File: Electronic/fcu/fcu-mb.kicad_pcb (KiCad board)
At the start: 2 copper layers, 114.3 x 71.1 mm, 48 parts, among them U1 MAX7219, U101 Connector-FPC-50pins, U2 MAX7219, U3 MAX7219

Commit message: Update fcu schemas and libraries
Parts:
- added J1: Conn_Coaxial_Power, Connector_Wire:SolderWirePad_1x02_P3.81mm_Drill1mm, F.Cu at (52.1, 123.8)
- moved R4 21.7 mm to (83.2, 118.7)
- moved R5 21.7 mm to (83.2, 122.6)
- moved R11 3.18 mm to (73.0, 115.6)
- moved R15 3.17 mm to (83.2, 111.8)
- moved U1 1.91 mm to (73.7, 79.4)
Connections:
- A1 pad 27: +5V -> Net-(A1-Pad27)
- A1 pad 30: Net-(A1-Pad30) -> +5V
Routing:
- net Dr3SegA: track 117.9 -> 174.4 mm, vias 2 -> 1
- net Dr3SegE: track 119.4 -> 97.1 mm
- net Dr3SegD: track 138.0 -> 154.5 mm, vias 1 -> 2
- net GND: track 271.1 -> 256.0 mm, vias 1 -> 0
- net Dr3SegB: track 107.4 -> 92.4 mm, vias 1 -> 2
- net Net-(R1-Pad2): track 47.9 -> 61.7 mm, vias 1 -> 0
- net speedAltF: track 36.3 -> 49.9 mm
- net BTN_GRP_2: track 154.8 -> 141.5 mm
- net hdgVsA: track 31.9 -> 44.6 mm
- net Dr3Dig5: track 38.7 -> 50.4 mm, vias 1 -> 2
- net speedAltDig3: track 39.1 -> 50.7 mm, vias 1 -> 0
- net speedAltDig5: track 59.0 -> 70.6 mm
- net Net-(K_AP2-Pad4): track 43.3 -> 54.7 mm
- net Net-(R17-Pad1): track 41.6 -> 52.3 mm, vias 0 -> 1
- net BTN_GRP_1: track 177.3 -> 166.8 mm
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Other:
- board size 114.3 x 71.1 mm -> 114.3 x 67.9 mm

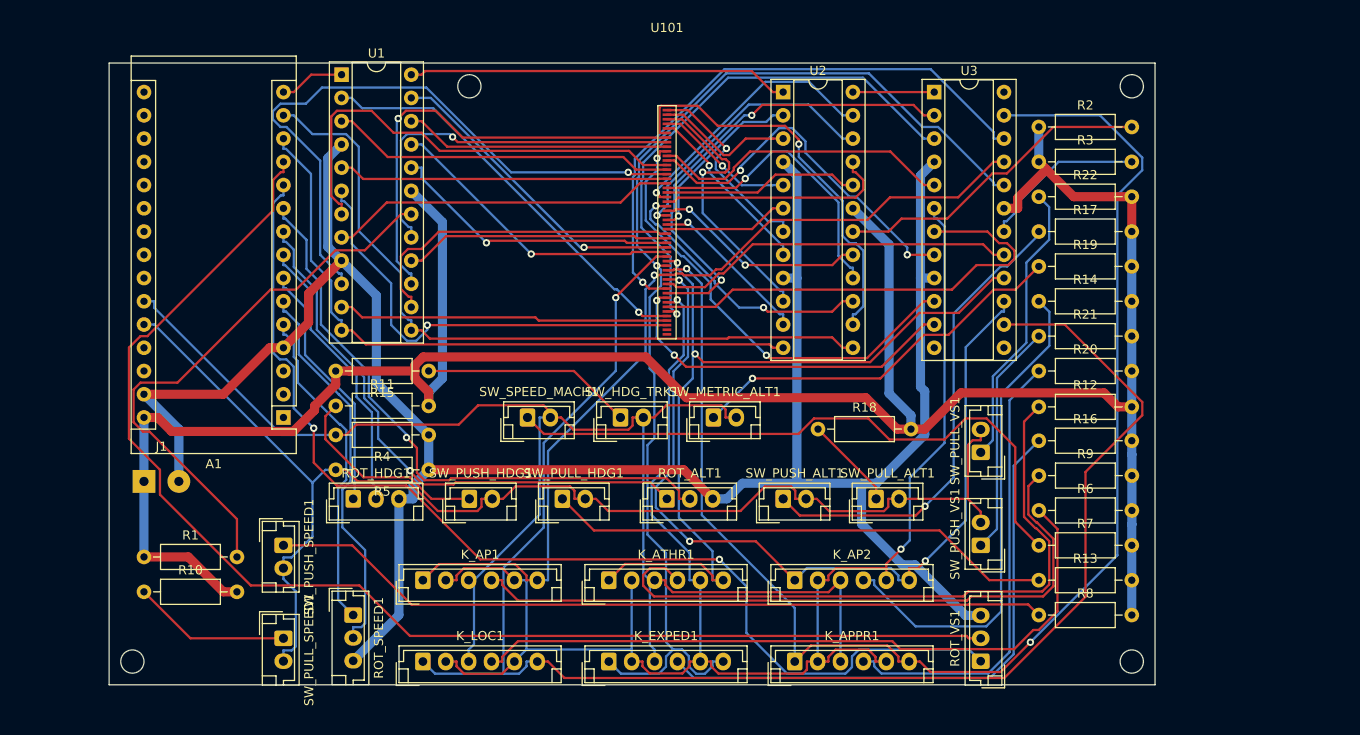
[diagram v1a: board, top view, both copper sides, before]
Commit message: Adust fcu display pcb layout Add Vcc to rotary encoder and update pcb with jst +1 pin
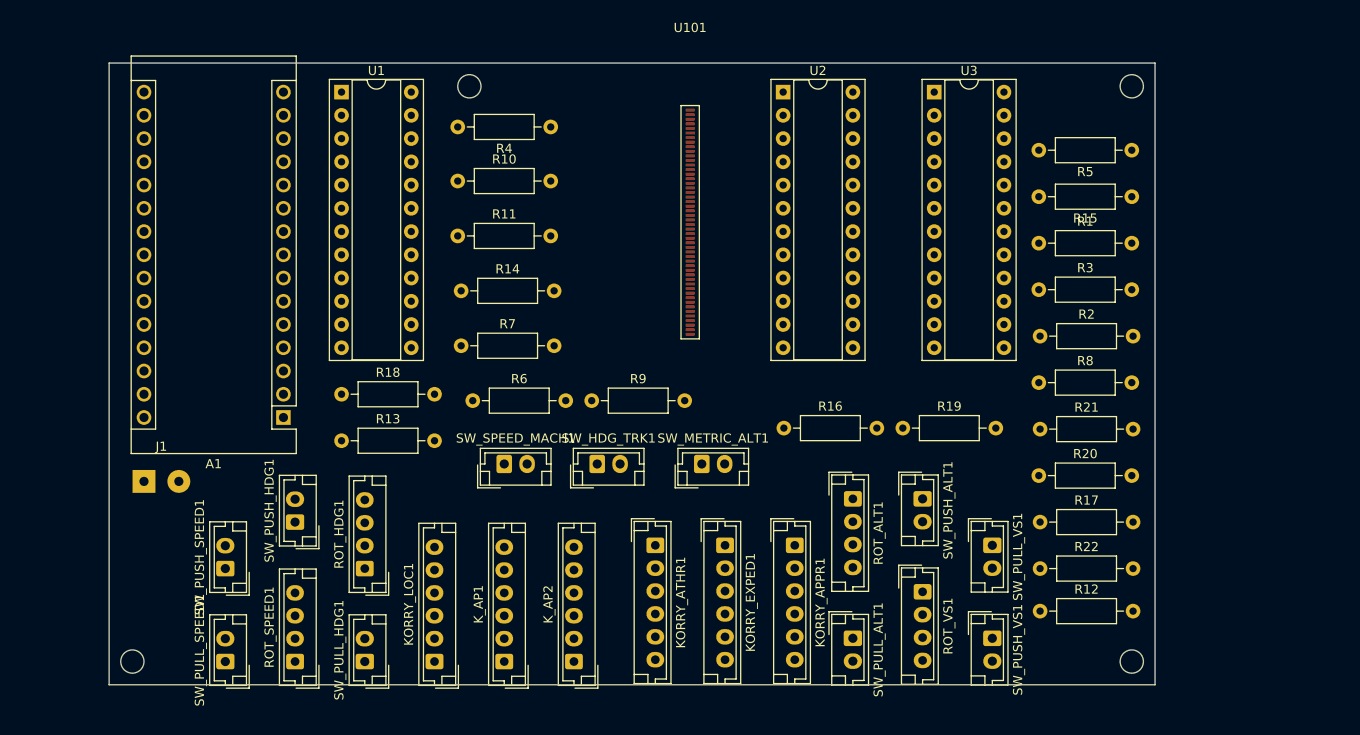
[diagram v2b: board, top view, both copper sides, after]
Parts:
- removed K_APPR1, K_ATHR1, K_EXPED1, K_LOC1: Korry, Connector_JST:JST_EH_B6B-EH-A_1x06_P2.50mm_Vertical
- added KORRY_APPR1: Korry, Connector_JST:JST_EH_B6B-EH-A_1x06_P2.50mm_Vertical, F.Cu at (123.2, 130.8)
- added KORRY_ATHR1: Korry, Connector_JST:JST_EH_B6B-EH-A_1x06_P2.50mm_Vertical, F.Cu at (108.0, 130.8)
- added KORRY_EXPED1: Korry, Connector_JST:JST_EH_B6B-EH-A_1x06_P2.50mm_Vertical, F.Cu at (115.6, 130.8)
- added KORRY_LOC1: Korry, Connector_JST:JST_EH_B6B-EH-A_1x06_P2.50mm_Vertical, F.Cu at (83.8, 143.5)
- ROT_ALT1, ROT_HDG1, ROT_SPEED1, ROT_VS1: footprint home-cockpit-footprints:JST_EH_B3B-EH-A_1x03_P2.50mm_Vertical_for_RotaryEncoder -> home-cockpit-footprints:JST_EH_B4B-EH-A_1x04_P2.50mm_Vertical_RotaryEncoder
- moved R1 103.6 mm to (149.9, 97.8)
- moved R5 84.4 mm to (160.0, 87.6)
- moved R15 79.2 mm to (160.0, 92.7)
- moved R13 77.7 mm to (73.7, 119.4)
- moved R7 66.8 mm to (86.7, 109.0)
- moved R14 63.1 mm to (86.7, 103.0)
- moved R6 63.0 mm to (88.0, 115.0)
- moved R10 56.5 mm to (86.4, 91.0)
- moved R18 52.2 mm to (73.7, 114.3)
- moved R9 49.6 mm to (101.0, 115.0)
- moved R22 40.6 mm to (150.0, 133.3)
- moved R4 36.2 mm to (96.5, 85.1)
- moved R17 31.8 mm to (150.0, 128.3)
- moved SW_PULL_HDG1 28.0 mm to (76.2, 143.5), turned to 90 degrees
- moved R16 27.9 mm to (122.0, 118.0)
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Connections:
- U3 pad 12: Net-(A1-Pad13) -> DriverLoad
- U3 pad 13: Net-(A1-Pad14) -> DriverClock
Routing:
- net +5V: track 271.1 -> 0.00 mm
- net GND: track 256.0 -> 0.00 mm
- net Dr3Dig2: track 188.5 -> 0.00 mm, vias 2 -> 0
- net Dr3SegA: track 174.4 -> 0.00 mm, vias 1 -> 0
- net BTN_GRP_1: track 166.8 -> 0.00 mm
- net Dr3SegD: track 154.5 -> 0.00 mm, vias 2 -> 0
- net ROT_VS_B: track 141.6 -> 0.00 mm
- net BTN_GRP_2: track 141.5 -> 0.00 mm
- net Dr3SegC: track 124.4 -> 0.00 mm, vias 1 -> 0
- net ROT_VS_A: track 120.9 -> 0.00 mm, vias 2 -> 0
- net Dr3SegE: track 97.1 -> 0.00 mm, vias 1 -> 0
- net Dr3SegF: track 95.9 -> 0.00 mm, vias 3 -> 0
- net Dr3SegB: track 92.4 -> 0.00 mm, vias 2 -> 0
- net Net-(R8-Pad1): track 85.7 -> 0.00 mm
- net DriverClock: track 81.4 -> 0.00 mm
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
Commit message: Update FCU PCB net routing
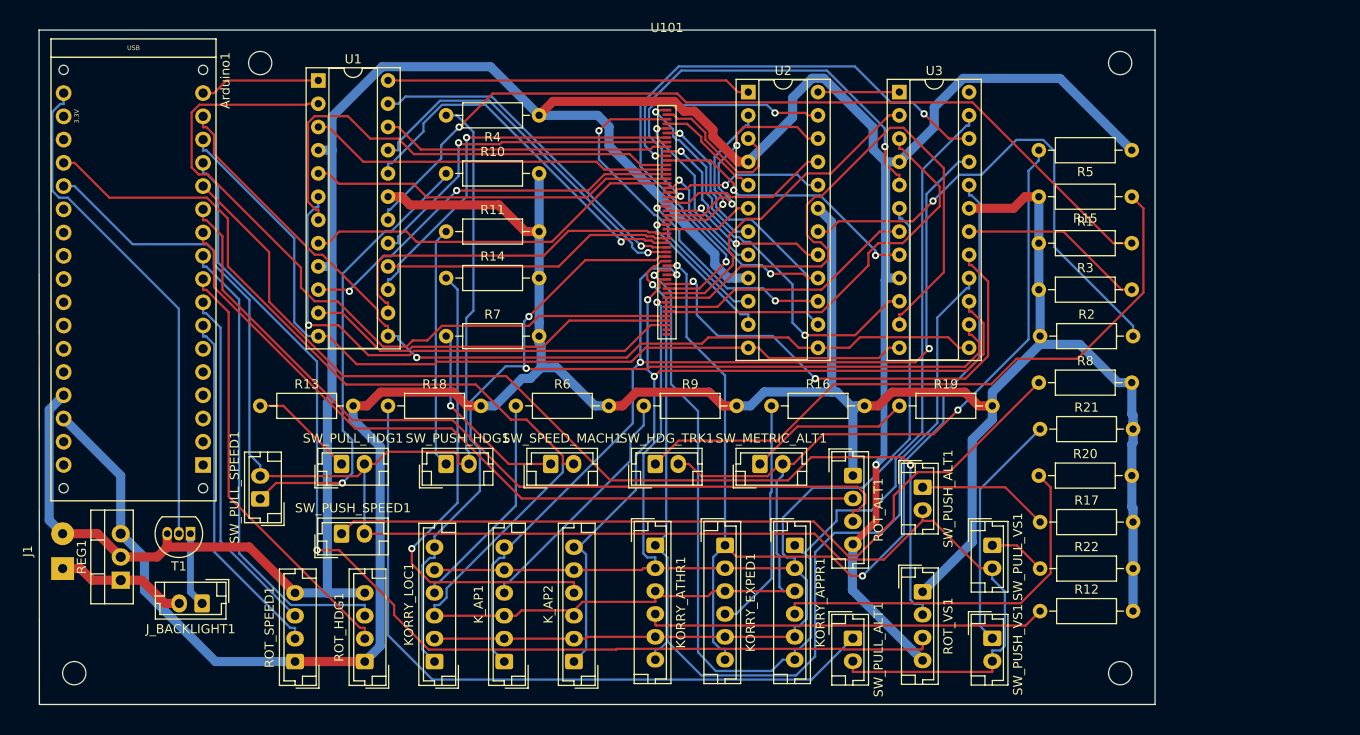
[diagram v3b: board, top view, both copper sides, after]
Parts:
- removed A1: Arduino_Nano_v3.x, Module:Arduino_Nano
- added Arduino1: Arduino_Nano_v3.x, home-cockpit-footprints:Arduino_Micro_Socket, F.Cu at (41.9, 77.5)
- added J_BACKLIGHT1: Conn_01x02_Male, Connector_JST:JST_EH_B2B-EH-A_1x02_P2.50mm_Vertical, F.Cu at (58.4, 137.2)
- added REG1: L7805, Package_TO_SOT_THT:TO-220-3_Vertical, F.Cu at (49.5, 134.6)
- added T1: BS170, Package_TO_SOT_THT:TO-92_Inline, F.Cu at (57.1, 129.5)
- moved SW_PULL_HDG1 21.7 mm to (73.7, 121.9), turned to 0 degrees
- moved SW_PULL_SPEED1 18.2 mm to (64.8, 125.7)
- moved SW_PUSH_HDG1 17.7 mm to (85.1, 121.9), turned to 0 degrees
- moved SW_PUSH_SPEED1 13.3 mm to (73.7, 129.5), turned to 0 degrees
- moved J1 13.0 mm to (43.2, 133.3), turned to 90 degrees
- moved ROT_HDG1 10.2 mm to (76.2, 143.5)
- moved R13 9.67 mm to (64.8, 115.6)
- moved SW_HDG_TRK1 6.35 mm to (108.0, 121.9)
- moved SW_METRIC_ALT1 6.35 mm to (119.4, 121.9)
- moved R9 5.71 mm to (106.7, 115.6)
- moved R18 5.24 mm to (78.7, 115.6)
- moved SW_SPEED_MACH1 5.08 mm to (96.5, 121.9)
- moved R6 4.74 mm to (92.7, 115.6)
- moved U2 3.81 mm to (118.1, 81.3)
- moved U3 3.81 mm to (134.6, 81.3)
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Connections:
- J1 pad 1: +5V -> +12V
- R4 pad 2: BTN_GRP_1 -> BTN_GRP_2
- R5 pad 2: BTN_GRP_2 -> BTN_GRP_1
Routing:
- net +5V: track 0.00 -> 319.4 mm
- net GND: track 0.00 -> 316.9 mm, vias 0 -> 1
- net BTN_GRP_2: track 0.00 -> 224.0 mm
- net BTN_GRP_1: track 0.00 -> 220.8 mm, vias 0 -> 1
- net Dr3Dig2: track 0.00 -> 170.0 mm, vias 0 -> 1
- net Dr3SegD: track 0.00 -> 128.8 mm, vias 0 -> 1
- net ROT_VS_B: track 0.00 -> 120.3 mm, vias 0 -> 1
- net Dr3SegB: track 0.00 -> 117.8 mm, vias 0 -> 1
- net Dr3SegA: track 0.00 -> 117.5 mm, vias 0 -> 2
- net Dr3SegC: track 0.00 -> 112.8 mm, vias 0 -> 2
- net ROT_VS_A: track 0.00 -> 112.6 mm, vias 0 -> 1
- net Dr3SegE: track 0.00 -> 111.0 mm, vias 0 -> 3
- net DriverClock: track 0.00 -> 100.3 mm, vias 0 -> 1
- net Net-(R1-Pad2): track 0.00 -> 95.3 mm, vias 0 -> 1
- net DriverLoad: track 0.00 -> 94.0 mm
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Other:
- board size 114.3 x 67.9 mm -> 122 x 73.7 mm

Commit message: Finalise first FCU PCB version
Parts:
- added R23: 100Ohms, Resistor_THT:R_Axial_DIN0207_L6.3mm_D2.5mm_P10.16mm_Horizontal, F.Cu at (149.4, 112.8)
- added R24: 100Ohms, Resistor_THT:R_Axial_DIN0207_L6.3mm_D2.5mm_P10.16mm_Horizontal, F.Cu at (63.4, 99.4)
- added R25: 100Ohms, Resistor_THT:R_Axial_DIN0207_L6.3mm_D2.5mm_P10.16mm_Horizontal, F.Cu at (135.0, 87.6)
- added R26: 100Ohms, Resistor_THT:R_Axial_DIN0207_L6.3mm_D2.5mm_P10.16mm_Horizontal, F.Cu at (93.3, 125.1)
- added R27: 100Ohms, Resistor_THT:R_Axial_DIN0207_L6.3mm_D2.5mm_P10.16mm_Horizontal, F.Cu at (149.4, 82.5)
- added R28: 100Ohms, Resistor_THT:R_Axial_DIN0207_L6.3mm_D2.5mm_P10.16mm_Horizontal, F.Cu at (135.0, 117.8)
- moved R13 89.2 mm to (149.4, 87.6)
- moved R2 88.9 mm to (63.4, 88.2)
- moved R1 86.6 mm to (63.4, 93.8)
- moved R8 86.6 mm to (63.4, 116.2)
- moved R18 72.9 mm to (149.4, 97.7)
- moved R4 50.7 mm to (145.2, 92.6)
- moved R15 46.1 mm to (122.5, 119.5)
- moved R9 43.6 mm to (63.4, 110.6)
- moved R22 40.7 mm to (149.4, 92.6)
- moved R14 35.3 mm to (112.3, 124.0)
- moved R16 31.5 mm to (149.4, 102.7)
- moved R6 31.2 mm to (63.4, 105.0)
- moved R11 30.3 mm to (97.9, 124.0)
- moved R12 30.3 mm to (149.4, 107.7)
- moved R17 25.4 mm to (135.0, 107.7)
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- renumbered U101 to DisplayConnector1, U2 to DriverHdgVs1, U3 to DriverOther1, U1 to DriverSpeedAlt1, K_AP1 to KORRY_AP1, K_AP2 to KORRY_AP2, J1 to PWR1
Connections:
- KORRY_AP1 pad 5: Dr3Dig2 -> GND
- KORRY_AP1 pad 6: Dr3SegE -> Net-(KORRY_AP1-Pad6)
- KORRY_AP2 pad 5: Dr3Dig2 -> GND
- KORRY_AP2 pad 6: Dr3SegF -> Net-(KORRY_AP2-Pad6)
- KORRY_APPR1 pad 5: Dr3Dig2 -> GND
- KORRY_APPR1 pad 6: Dr3SegD -> Net-(KORRY_APPR1-Pad6)
- KORRY_ATHR1 pad 5: Dr3Dig2 -> GND
- KORRY_ATHR1 pad 6: Dr3SegB -> Net-(KORRY_ATHR1-Pad6)
- KORRY_EXPED1 pad 5: Dr3Dig2 -> GND
- KORRY_EXPED1 pad 6: Dr3SegC -> Net-(KORRY_EXPED1-Pad6)
- KORRY_LOC1 pad 5: Dr3Dig2 -> GND
- KORRY_LOC1 pad 6: Dr3SegA -> Net-(KORRY_LOC1-Pad6)
- ROT_ALT1 pad 1: +5V -> (no net)
- ROT_HDG1 pad 1: +5V -> (no net)
- ROT_SPEED1 pad 1: +5V -> (no net)
- ROT_VS1 pad 1: +5V -> (no net)
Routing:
- net GND: track 316.9 -> 0.00 mm, vias 1 -> 0
- net hdgVsDig1: track 16.6 -> 119.6 mm, vias 1 -> 0
- net Net-(R13-Pad1): track 11.5 -> 110.1 mm
- net Net-(DriverSpeedAlt1-Pad18): track 95.3 -> 16.2 mm, vias 1 -> 0
- net Net-(KORRY_LOC1-Pad6): track 0.00 -> 78.3 mm
- net Net-(KORRY_ATHR1-Pad6): track 0.00 -> 74.7 mm, vias 0 -> 1
- net Net-(R8-Pad1): track 87.6 -> 18.8 mm
- net Net-(KORRY_EXPED1-Pad6): track 0.00 -> 60.6 mm
- net Dr3Dig1: track 66.3 -> 8.33 mm
- net Dr3Dig2: track 170.0 -> 115.2 mm
- net Net-(R15-Pad1): track 72.1 -> 21.2 mm
- net Net-(KORRY_AP1-Pad6): track 0.00 -> 50.6 mm
- net Net-(R18-Pad1): track 79.7 -> 30.8 mm
- net Dr3SegC: track 112.8 -> 65.6 mm, vias 2 -> 1
- net Net-(R22-Pad1): track 6.27 -> 49.0 mm
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- added copper zone on B.Cu, net GND
- added copper zone on F.Cu, net GND
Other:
- board text added: "HomeCockpit A320 - VirtualGit FCU MotherBoard V1.0 - 17/02/2021"
